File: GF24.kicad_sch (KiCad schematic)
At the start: 67 parts, among them J1 USB4110GFA, J2 S2B-PH-SM4-TB, J3 Conn_01x06_Pin, J4 Conn_ARM_SWD_TagConnect_TC2030, J5 Conn_01x04_Pin, J6 Conn_01x06_Pin, Q1 3904, SW4 BOOT, U1 TPS79533DCQR, U2 LTC1733, U3 SAM-M10Q, U4 STM32F102C8Tx, X1 ECS-2520MV-160-CN

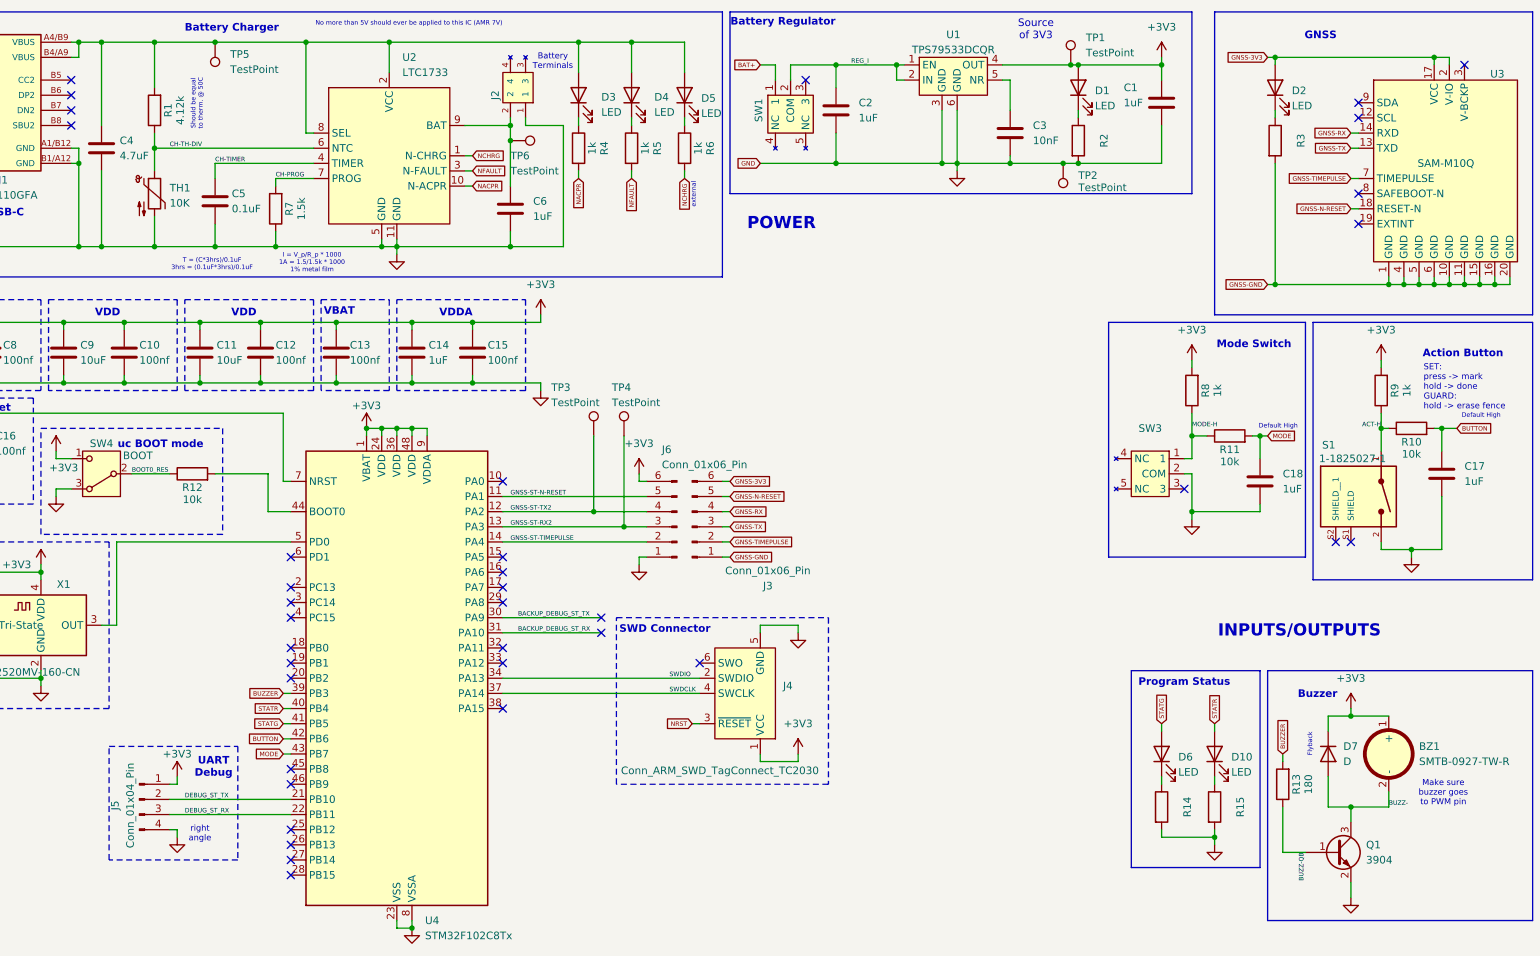
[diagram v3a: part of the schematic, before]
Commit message: need to finish placement but this is an almost completed R2
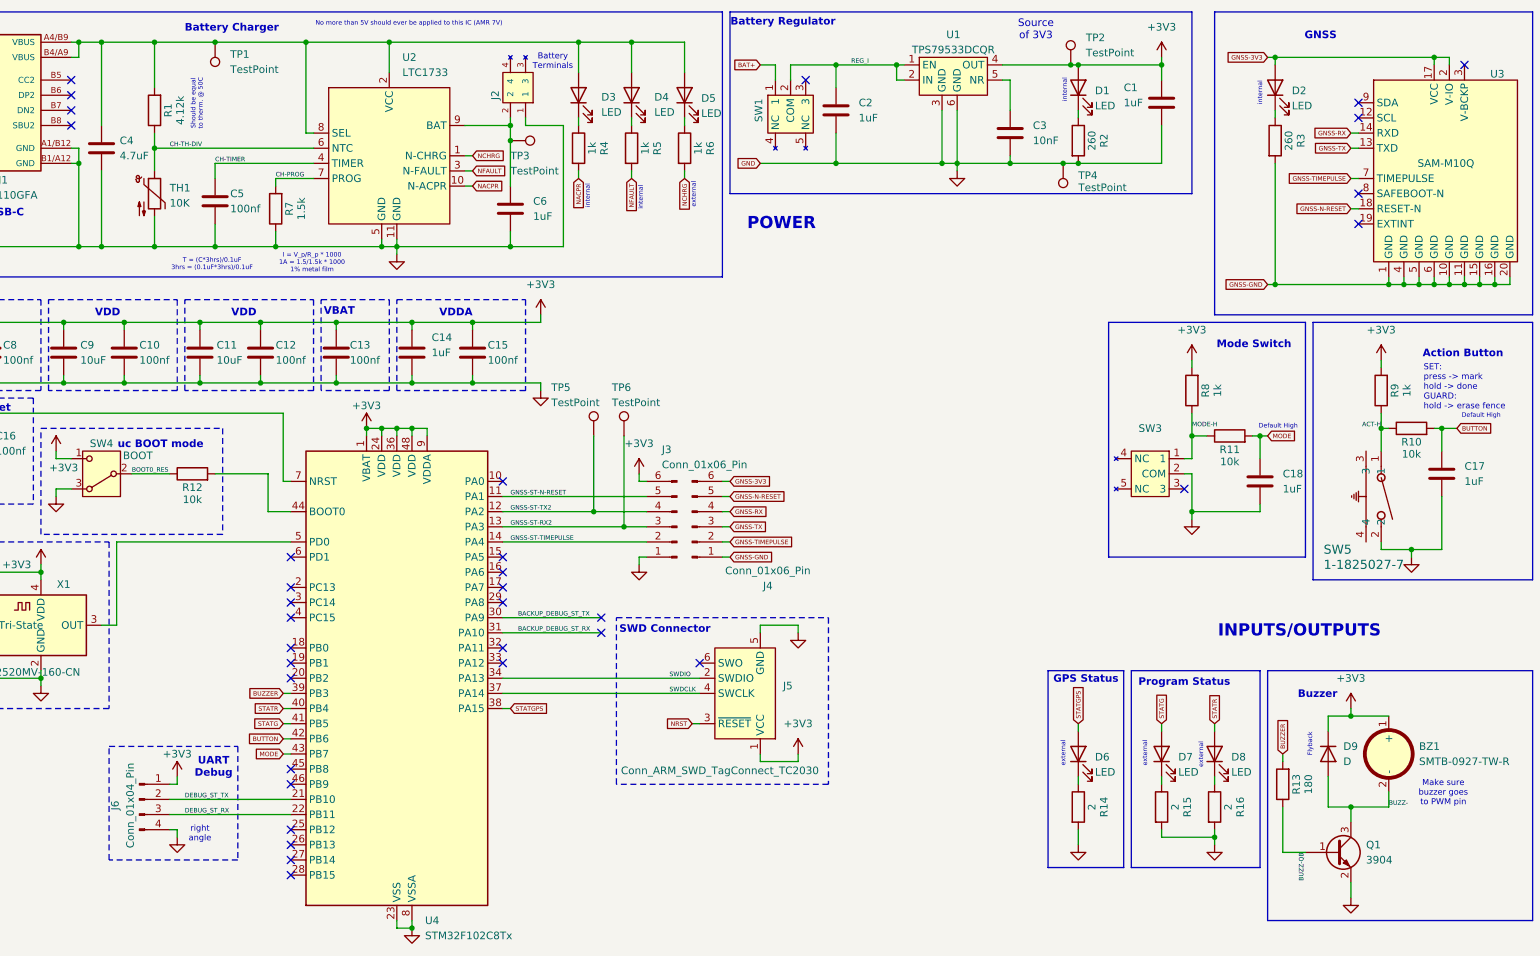
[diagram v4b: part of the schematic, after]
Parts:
- removed S1: 1-1825027-1, MB-SW:SW_1-1825027-1, symbol MB-SW:1-1825027-1
- added D6: LED, MB-Opto:WE-1204-Mono-Side, symbol Device:LED
- added R14: 2, MB-Generic:R0603_medium, symbol Device:R
- added SW5: 1-1825027-7, MB-SW:SW2_1825027-F_TEC, symbol MB-SW:1-1825027-7
- BZ1: Distributor Link (none) -> https://www.digikey.com/en/products/detail/pui-audio-inc/sm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; Manufacturer (none) -> PUI Audio, Inc.; Manufacturer PN (none) -> 668-SMTB-0927-TW-RTR-ND
- C1, C17, C18, C2, C6: footprint MB-Generic:C0805_medium -> Capacitor_SMD:C_1210_3225Metric; Distributor Link https://www.digikey.com/en/products/detail/kemet/c0805c105k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 -> https://www.digikey.com/en/products/detail/kemet/C1210C105K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; Manufacturer PN C0805C105K8RACTU -> 399-13217-2-ND
- C10, C12, C13, C15, C16, C19, C8: footprint MB-Generic:C1206_medium -> Capacitor_SMD:C_0805_2012Metric; Distributor Link https://www.digikey.com/en/products/detail/kemet/C1206C475K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 -> https://www.digikey.com/en/products/detail/kemet/C0805C104K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; Manufacturer PN C1206C475K8RACTU -> 399-C0805C104K8RACTUTR-ND
- C11, C7, C9: footprint MB-Generic:C1206_medium -> Capacitor_SMD:C_1210_3225Metric; Distributor Link https://www.digikey.com/en/products/detail/kemet/C1206C475K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 -> https://www.digikey.com/en/products/detail/kemet/C1210C106K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; Manufacturer PN C1206C475K8RACTU -> 399-C1210C106K8RACTUTR-ND
- C14: footprint MB-Generic:C1206_medium -> Capacitor_SMD:C_1210_3225Metric; Distributor Link https://www.digikey.com/en/products/detail/kemet/C1206C475K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 -> https://www.digikey.com/en/products/detail/kemet/C1210C105K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; Manufacturer PN C1206C475K8RACTU -> 399-13217-2-ND
- C3: footprint MB-Generic:C0402_medium -> Capacitor_SMD:C_0603_1608Metric; Distributor Link https://www.digikey.com/en/products/detail/kemet/c0402c103k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 -> https://www.digikey.com/en/products/detail/kemet/C0603C103K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; Manufacturer PN C0402C103K8RACTU -> 399-C0603C103K8RACTUTR-ND
- C4: footprint MB-Generic:C1206_medium -> Capacitor_SMD:C_1210_3225Metric; Distributor Link https://www.digikey.com/en/products/detail/kemet/C1206C475K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 -> https://www.digikey.com/en/products/detail/kemet/C1210C475K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; Manufacturer PN C1206C475K8RACTU -> 399-C1210C475K8RACTUTR-ND
- C5: value 0.1uF -> 100nf; footprint MB-Generic:C0603_medium -> Capacitor_SMD:C_0805_2012Metric; Distributor Link https://www.digikey.com/en/products/detail/kemet/c0603c104k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 -> https://www.digikey.com/en/products/detail/kemet/C0805C104K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; Manufacturer PN C0603C104K8RACTU -> 399-C0805C104K8RACTUTR-ND
- D1, D2, D3, D4: footprint (none) -> MB-Opto:WE-0603-Mono-Chip-Advance; Distributor Link (none) -> https://www.digikey.com/en/products/detail/w%C3%BCrth-elekt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; Manufacturer PN (none) -> 732-150060RS75003TR-ND
- D5: footprint (none) -> MB-Opto:WE-1204-Mono-Side; Distributor Link (none) -> https://www.digikey.com/en/products/detail/w%C3%BCrth-elekt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; Manufacturer PN (none) -> 732-5024-2-ND
- D7: renamed from D6; footprint (none) -> MB-Opto:WE-1204-Mono-Side; Distributor Link (none) -> https://www.digikey.com/en/products/detail/w%C3%BCrth-elekt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; Manufacturer PN (none) -> 732-5024-2-ND
- D8: renamed from D10; footprint (none) -> MB-Opto:WE-1204-Mono-Side; Distributor Link (none) -> https://www.digikey.com/en/products/detail/w%C3%BCrth-elekt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; Manufacturer PN (none) -> 732-5024-2-ND
- D9: renamed from D7; Manufacturer PN MMSD4148T1G -> MMSD4148T1GOSTR-ND
- J1: Manufacturer PN USB4110-GF-A -> 2073-USB4110-GF-A-2-ND
- J2: Manufacturer PN S2B-PH-SM4-TB -> 455-S2B-PH-SM4-TBTR-ND
- J3: renamed from J6; footprint (none) -> Connector_PinHeader_1.00mm:PinHeader_1x06_P1.00mm_Vertical; Distributor Link (none) -> https://www.digikey.com/en/products/detail/sullins-connecto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; Manufacturer PN (none) -> S7039-ND
- J4: renamed from J3; footprint (none) -> Connector_PinHeader_1.00mm:PinHeader_1x06_P1.00mm_Vertical; Distributor Link (none) -> https://www.digikey.com/en/products/detail/w%C3%BCrth-elekt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; Manufacturer PN (none) -> 732-5319-ND
- J6: renamed from J5; footprint (none) -> Connector_PinHeader_1.00mm:PinHeader_1x04_P1.00mm_Vertical; Distributor Link (none) -> https://www.digikey.com/en/products/detail/sullins-connecto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; Manufacturer PN (none) -> S9016E-04-ND
- Q1: Manufacturer PN MMBT3904LT1G -> MMBT3904LT1GOSTR-ND
- R1: Manufacturer PN RC0603FR-074K12L -> 311-4.12KHRTR-ND
- R10, R11, R12: Manufacturer PN RC0603FR-0710KL -> 311-10.0KHRTR-ND
- R13: Manufacturer PN RC0603FR-07180RL -> 311-180HRTR-ND
- R15: renamed from R14; value ~ -> 2; Distributor Link (none) -> https://www.digikey.com/en/products/detail/yageo/RC0603JR-0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; Manufacturer PN (none) -> 13-RC0603JR-072RLTR-ND
- R16: renamed from R15; value ~ -> 2; Distributor Link (none) -> https://www.digikey.com/en/products/detail/yageo/RC0603JR-0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; Manufacturer PN (none) -> 13-RC0603JR-072RLTR-ND
- R2, R3: value ~ -> 260; Distributor Link (none) -> https://www.digikey.com/en/products/detail/yageo/RC0603FR-0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; Manufacturer PN (none) -> 311-261HRTR-ND
- R4, R5, R6: Distributor Link (none) -> https://www.digikey.com/en/products/detail/yageo/rc0603fr-0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; Manufacturer PN (none) -> 311-1.00KHRTR-ND
- R7: Manufacturer PN RC0603FR-071K5L -> 311-1.50KHRTR-ND
- R8, R9: Manufacturer PN RC0603FR-071KL -> 311-1.00KHRTR-ND
- SW1, SW3: Manufacturer PN 500ASSP1SM6QE -> EG5810TR-ND
- SW2: Manufacturer PN PTS815SJM250SMTRLFS -> CKN12215-2-ND
- SW4: Manufacturer PN CJS-1200TA -> 563-1021-2-ND
- TH1: Manufacturer PN NCU18XH103F6SRB -> 490-18139-2-ND
- TP1: renamed from TP5; footprint (none) -> TestPoint:TestPoint_Pad_D2.5mm
- TP2: renamed from TP1; footprint (none) -> TestPoint:TestPoint_Pad_D2.5mm
- TP3: renamed from TP6; footprint (none) -> TestPoint:TestPoint_Pad_D2.5mm
- TP4: renamed from TP2; footprint (none) -> TestPoint:TestPoint_Pad_D2.5mm
- TP5: renamed from TP3; footprint (none) -> TestPoint:TestPoint_Pad_D2.5mm
- TP6: renamed from TP4; footprint (none) -> TestPoint:TestPoint_Pad_D2.5mm
- U1: Distributor Link (none) -> https://www.digikey.com/en/products/detail/texas-instrument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; Manufacturer PN (none) -> 296-13810-2-ND
- U2: Manufacturer PN LTC1733EMSE#TRPBF -> LTC1733EMSE#TRPBFTR-ND
- U3: Manufacturer PN SAM-M10Q-00B -> 672-SAM-M10Q-00BTR-ND
- U4: Distributor Link (none) -> https://www.digikey.com/en/products/detail/stmicroelectroni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; Manufacturer PN (none) -> 497-8307-ND
- X1: Distributor Link (none) -> https://www.digikey.com/en/products/detail/ecs-inc/ecs-2520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; Manufacturer PN (none) -> XC3030TR-ND
- renumbered J4 to J5
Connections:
- net ACT-H: now also SW5.1
- net GND: now also R14.2, SW5.2
- net STATGPS: now reaches U4.38 (PA15)
- net STATGPS: now also D6.2 (A)
- new net: D6.1 (K), R14.1
- no-connect marks 42 -> 39
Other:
- note added: "GPS Status"
- note added: "internal"

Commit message: going to make some changes to the I/O
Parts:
- J3: footprint Connector_PinHeader_1.00mm:PinHeader_1x06_P1.00mm_Vertical -> Connector_PinSocket_2.54mm:PinSocket_1x06_P2.54mm_Vertical
- J4: footprint Connector_PinHeader_1.00mm:PinHeader_1x06_P1.00mm_Vertical -> Connector_PinHeader_2.54mm:PinHeader_1x06_P2.54mm_Vertical
- J6: footprint Connector_PinHeader_1.00mm:PinHeader_1x04_P1.00mm_Vertical -> Connector_PinHeader_2.54mm:PinHeader_1x04_P2.54mm_Vertical
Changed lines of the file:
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@@
 			)
 		)
-		(property "Footprint" "Connector_PinHeader_1.00mm:PinHeader_1x06_P1.00mm_Vertical"
+		(property "Footprint" "Connector_PinSocket_2.54mm:PinSocket_1x06_P2.54mm_Vertical"
 			(at 140.97 99.06 0)
 			(effects
@@
 			)
 		)
-		(property "Footprint" "Connector_PinHeader_1.00mm:PinHeader_1x06_P1.00mm_Vertical"
+		(property "Footprint" "Connector_PinHeader_2.54mm:PinHeader_1x06_P2.54mm_Vertical"
 			(at 143.51 99.06 0)
 			(effects
@@
 			)
 		)
-		(property "Footprint" "Connector_PinHeader_1.00mm:PinHeader_1x04_P1.00mm_Vertical"
+		(property "Footprint" "Connector_PinHeader_2.54mm:PinHeader_1x04_P2.54mm_Vertical"
 			(at 50.8 144.78 0)
 			(effects

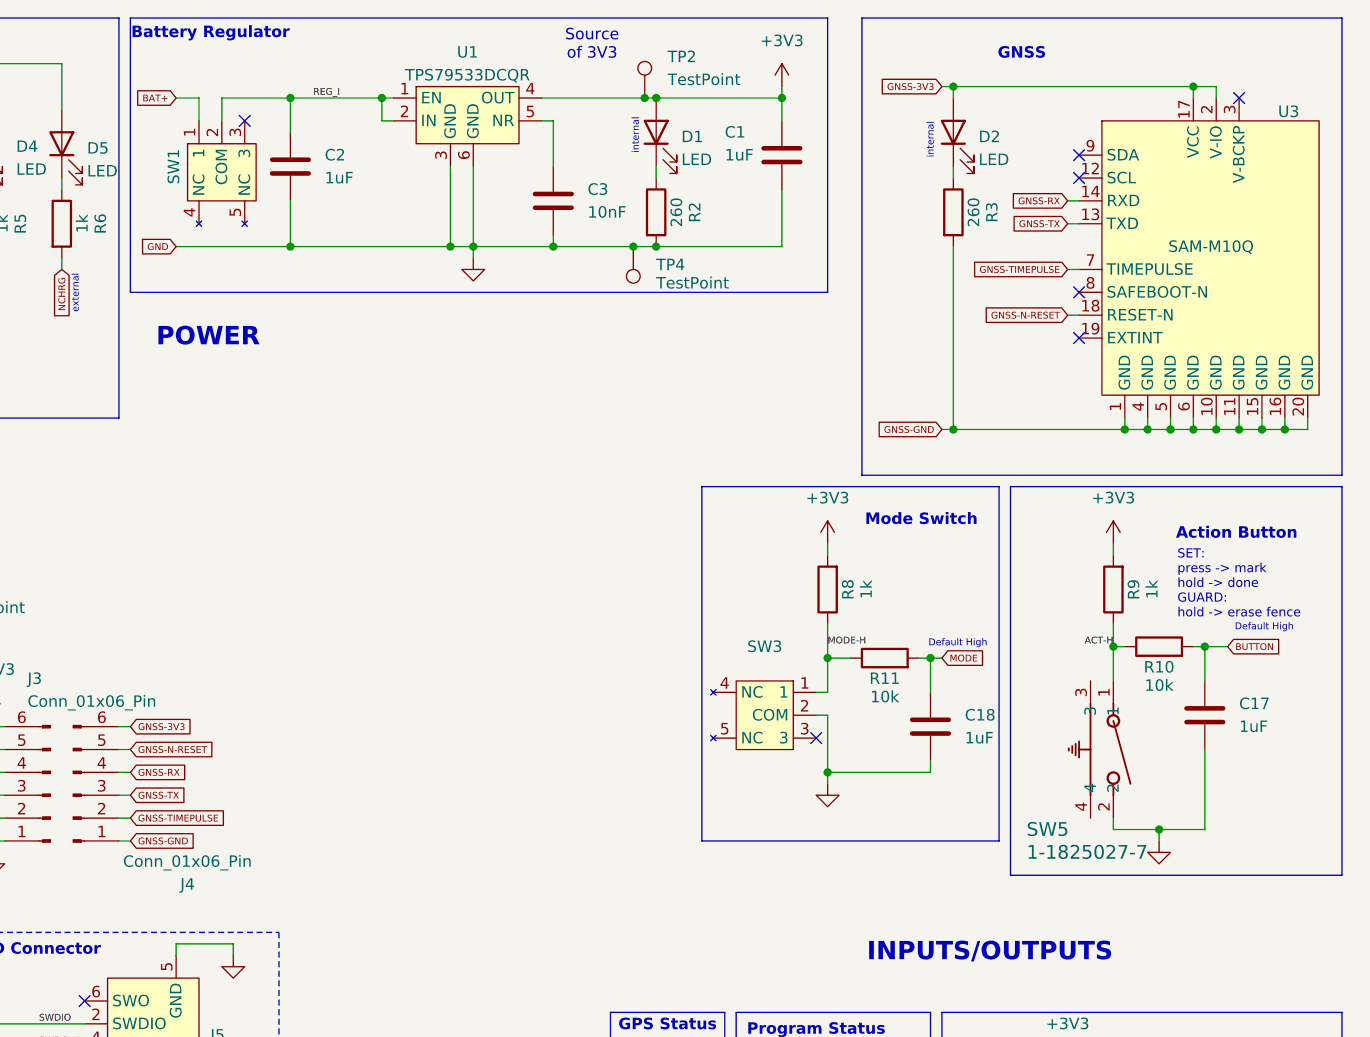
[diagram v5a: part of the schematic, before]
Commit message: added Wago
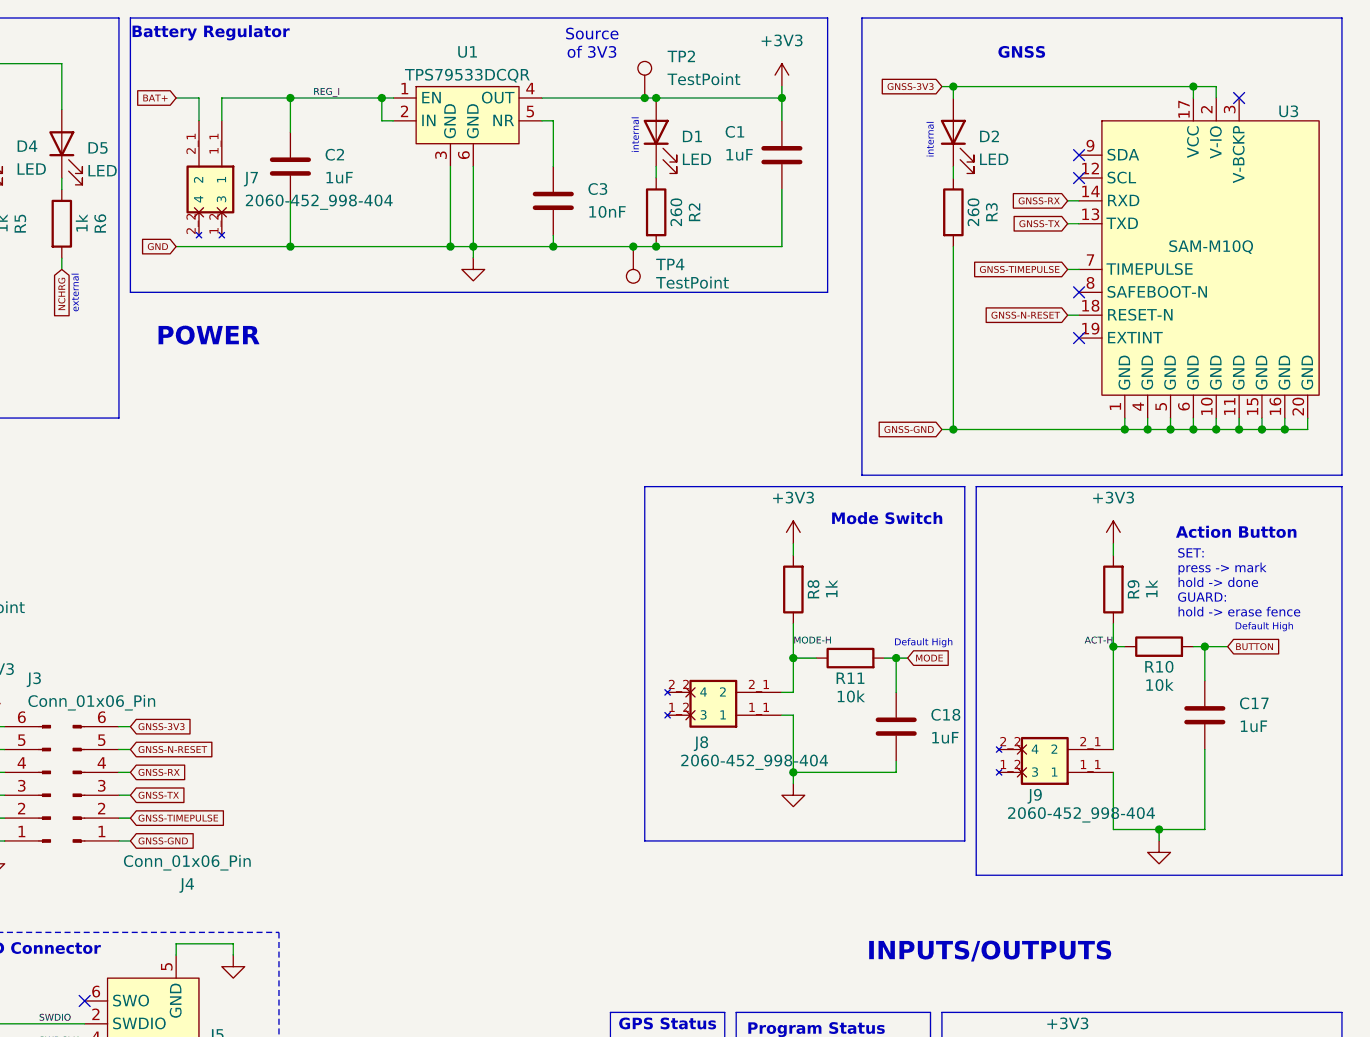
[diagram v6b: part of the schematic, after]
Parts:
- removed SW1, SW3: ~, MB-SW:SW_500ASSP1SM6QE, symbol MB-SW:SW_500ASSP1SM6QE
- removed SW5: 1-1825027-7, MB-SW:SW2_1825027-F_TEC, symbol MB-SW:1-1825027-7
- added J7, J8, J9: 2060-452_998-404, MB-Conn:WAGO_2060-452_998-404, symbol MB-Conn:2060-452_998-404
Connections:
- net ACT-H: now also J9.2_1 (2)
- net BAT+: now also J7.2_1 (2)
- net GND: now also J8.1_1 (1), J9.1_1 (1)
- net MODE-H: now also J8.2_1 (2)
- net REG_I: now also J7.1_1 (1)
- no-connect marks 39 -> 37
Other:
- moved on the sheet: C18, R11, R8

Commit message: 3D done, started routing
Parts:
- removed J2: S2B-PH-SM4-TB, MB-Conn:JST_S2B-PH-SM4-TB, symbol MB-Conn:S2B-PH-SM4-TB
- removed J3: Conn_01x06_Pin, Connector_PinSocket_2.54mm:PinSocket_1x06_P2.54mm_Vertical, symbol Connector:Conn_01x06_Pin
- removed J4: Conn_01x06_Pin, Connector_PinHeader_2.54mm:PinHeader_1x06_P2.54mm_Vertical, symbol Connector:Conn_01x06_Pin
- removed J7, J8, J9: 2060-452_998-404, MB-Conn:WAGO_2060-452_998-404, symbol MB-Conn:2060-452_998-404
- added BT1: Battery_Cell, MB-SW:Solder_Joint_1_2, symbol Device:Battery_Cell
- added SW1, SW4: EG1205, MB-SW:Solder_Joint_1_2, symbol Switch:SW_SPST
- added SW5: 360-2674-ND, MB-SW:Solder_Joint_1_2, symbol Switch:SW_SPST
- C1, C14, C17, C18, C2, C6: footprint Capacitor_SMD:C_1210_3225Metric -> Capacitor_SMD:C_0603_1608Metric
- C11, C4, C7, C9: footprint Capacitor_SMD:C_1210_3225Metric -> Capacitor_SMD:C_0805_2012Metric
- J4: renamed from J6; footprint Connector_PinHeader_2.54mm:PinHeader_1x04_P2.54mm_Vertical -> Connector_PinHeader_2.54mm:PinHeader_1x04_P2.54mm_Horizontal
- TP1, TP2, TP3, TP4, TP5, TP6: footprint TestPoint:TestPoint_Pad_D2.5mm -> TestPoint:TestPoint_Pad_D1.5mm
- renumbered J5 to J3, SW4 to SW3
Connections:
- net GNSS-3V3 is gone; now on net +3V3: D2.2 (A), U3.17 (VCC), U3.2 (V-IO)
- net GNSS-GND is gone; now on net GND: R3.2, U3.1 (GND), U3.10 (GND), U3.11 (GND), U3.15 (GND), U3.16 (GND), U3.20 (GND), U3.4 (GND), U3.5 (GND), U3.6 (GND)
- net GNSS-ST-N-RESET is gone; now on net GNSS-N-RESET: U4.11 (PA1)
- net GNSS-ST-RX2 is gone; now on net GNSS-TX: TP6.1, U4.13 (PA3)
- net GNSS-ST-TIMEPULSE is gone; now on net GNSS-TIMEPULSE: U4.14 (PA4)
- net GNSS-ST-TX2 is gone; now on net GNSS-RX: TP5.1, U4.12 (PA2)
- net ACT-H: now also SW5.1 (A)
- net BAT+: now also C6.1, TP3.1, U2.9 (BAT), BT1.1 (+), SW1.1 (A)
- net GND: now also BT1.2 (-), SW4.2 (B), SW5.2 (B)
- net MODE-H: now also SW4.1 (A)
- net REG_I: now also SW1.2 (B)
- net USBC+: now reaches C4.1, D3.2 (A), D4.2 (A), D5.2 (A), J1.A4/B9 (VBUS), J1.B4/A9 (VBUS), R1.2, TP1.1, U2.2 (VCC), U2.8 (SEL)
- net CLK_OUT: now reaches U4.5 (PD0), X1.3 (OUT)
- net Noise_Reduction: now reaches C3.1, U1.5 (NR)
- net BOOT0_I: now reaches R12.2, U4.44 (BOOT0)
